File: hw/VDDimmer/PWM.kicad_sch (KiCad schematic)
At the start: 23 parts, among them J3 CH1 V+/LED-, J4 CH2 V+/LED-, J5 CH3 V+/LED-, J6 CH4 V+/LED-, Q1 20N06, Q2 20N06, Q3 20N06, Q4 20N06, U4 74HCT125

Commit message: Schematic pass: MPN/LCSC/Manufacturer on all 79 sourced parts
F1 -> "8A 250V", U3 -> "BL1117-33CX", J2 -> "VIN 12V" (was "VIN 9-24V",
which invited 24 V into an 18 V TVS). R11/R12 values cleaned to "47R" with
the DNP intent moved into the Assembly field. ERC still 0 violations.

Every sourced part now carries MPN, LCSC and Manufacturer, plus an Assembly
note anywhere the choice needs explaining - why D5 is an SMBJ18A, why R30's
current rating still needs checking, why L1 is candidate-only.

Two things this pass could NOT do, both because no MCP tool writes them:

- KiCad's (dnp yes) attribute. R11 and R12 must be flagged in the GUI; their
  Assembly fields say so. All five text-only DNPs were in this state, but
  L3/C20/R31 are now fitted by decision, so only R11/R12 remain.
- Fields on units 2-5 of a multi-unit symbol. Konnect writes unit 1 only,
  where the GUI propagates to all units. U4/U5 are 5-unit 74HCT125s, so
  grouping a BOM by MPN splits U5 into two lines and would order 3 of a
  2-off part. tools/export-bom.sh groups by Value+Footprint instead, which
  collapses correctly - 49 lines, 96 parts, and the 15 lines without an LCSC
  are exactly the mounting holes and hand-fit connectors.

Also checked and left alone: the U4/U5 symbol's lib_id is 74AHCT125 while its
value is 74HCT125. AHCT would be the conventional WS2812 level shifter, but
JLC has 70 of it in SO-14 against 88,003 of the HCT part, and HCT is fine here
- TTL inputs, 15 ns against 300 ns bit times. The value is the buyable intent.

Co-Authored-By: Claude Opus 5 (1M context) <noreply@anthropic.com>
Claude-Session: https://claude.ai/code/session_01QsYnM2qRBWQsyKPH1v7rLR
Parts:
- C50: LCSC (none) -> C15850; MPN (none) -> CL21A106KAYNNNE; Manufacturer (none) -> Samsung Electro-Mechanics
- C51: LCSC (none) -> C14663; MPN (none) -> CC0603KRX7R9BB104; Manufacturer (none) -> YAGEO
- D1, D2, D3, D4: LCSC (none) -> C8678; MPN (none) -> SS34; Manufacturer (none) -> MDD
- Q1: Assembly (none) -> Rds(on) 29 mOhm at the 4.5 V the 74HCT125 drives, not the 1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; LCSC (none) -> C2890395; MPN (none) -> 20N06; Manufacturer (none) -> UMW
- Q2, Q3, Q4: LCSC (none) -> C2890395; MPN (none) -> 20N06; Manufacturer (none) -> UMW
- R1, R2, R3, R4: LCSC (none) -> C17557; MPN (none) -> 0805W8F2200T5E; Manufacturer (none) -> UNI-ROYAL
- R5, R6, R7, R8: LCSC (none) -> C17414; MPN (none) -> 0805W8F1002T5E; Manufacturer (none) -> UNI-ROYAL
- U4: LCSC (none) -> C5962; MPN (none) -> 74HCT125D,653; Manufacturer (none) -> Nexperia

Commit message: Fix six drill defects, fit the I2C pull-ups, add the board ID
Drill defects
-------------
hole_to_hole and holes_co_located are downgraded to warning in .kicad_pro, so
the board reported "DRC 0 errors" while carrying five hole_to_hole and one
holes_co_located -- two of them with physically overlapping drills. Same shape
of trap as the split-net lesson already in HANDOFF.

Five vias deleted, each proven non-load-bearing first by checking which track
endpoints actually land on it. In every overlapping pair only one via carried a
track; the other was a bare stitching via with its twin 0.1-0.5 mm away.
d85c5d26 was redundant by construction -- 1 mm from J2's PTH GND pad, which
already ties both layers. afb88017 was an exact duplicate of a14092cd.
Afterwards GND is still one connected group, the split-net count is unchanged
at 12, and via count went 192 -> 187.

I2C pull-ups (R45, R46)
-----------------------
4.7k 0805, C17673, per the 2026-08-29 decision. Verified against the exported
netlist rather than the tools' return values, because the pins are tied with a
plain +3V3 net label -- the convention J13's own supply pin uses on this sheet.
Had that not merged with the power net the pull-ups would have pulled to
nothing, which is the silent failure the decision existed to prevent.

  +3V3          15 nodes  ... J13.1 R43.1 R44.1 R45.1 R46.1 U1.2 U3.2
  /MCU/I2C_SDA   3 nodes  J13.3  R45.2  U1.20
  /MCU/I2C_SCL   3 nodes  J13.4  R46.2  U1.18

The taps run on B.Cu because ADDR1_DIN crosses the whole board on F.Cu at
y=96.33, x 149.35-168.60, walling +3V3 (which reaches J13.1 at y=95) off from
the I2C lines at y=100.14 and 102.67. There is no F.Cu-only path; going round
its east end costs ~30 mm and still needs via hops over the GATE_IN verticals.
B.Cu there is bare GND pour and J13's pads 1/3/4 are through-hole, so they are
reachable from below with no via at that end.

Both parts are rotated 180 deg. They arrive with pad 1 (+3V3) west, which would
force the SDA return to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
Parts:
- U4: LCSC (none) -> C5962; MPN (none) -> 74HCT125D,653; Manufacturer (none) -> Nexperia
- U4: LCSC C5962 -> (none); MPN 74HCT125D,653 -> (none); Manufacturer Nexperia -> (none)

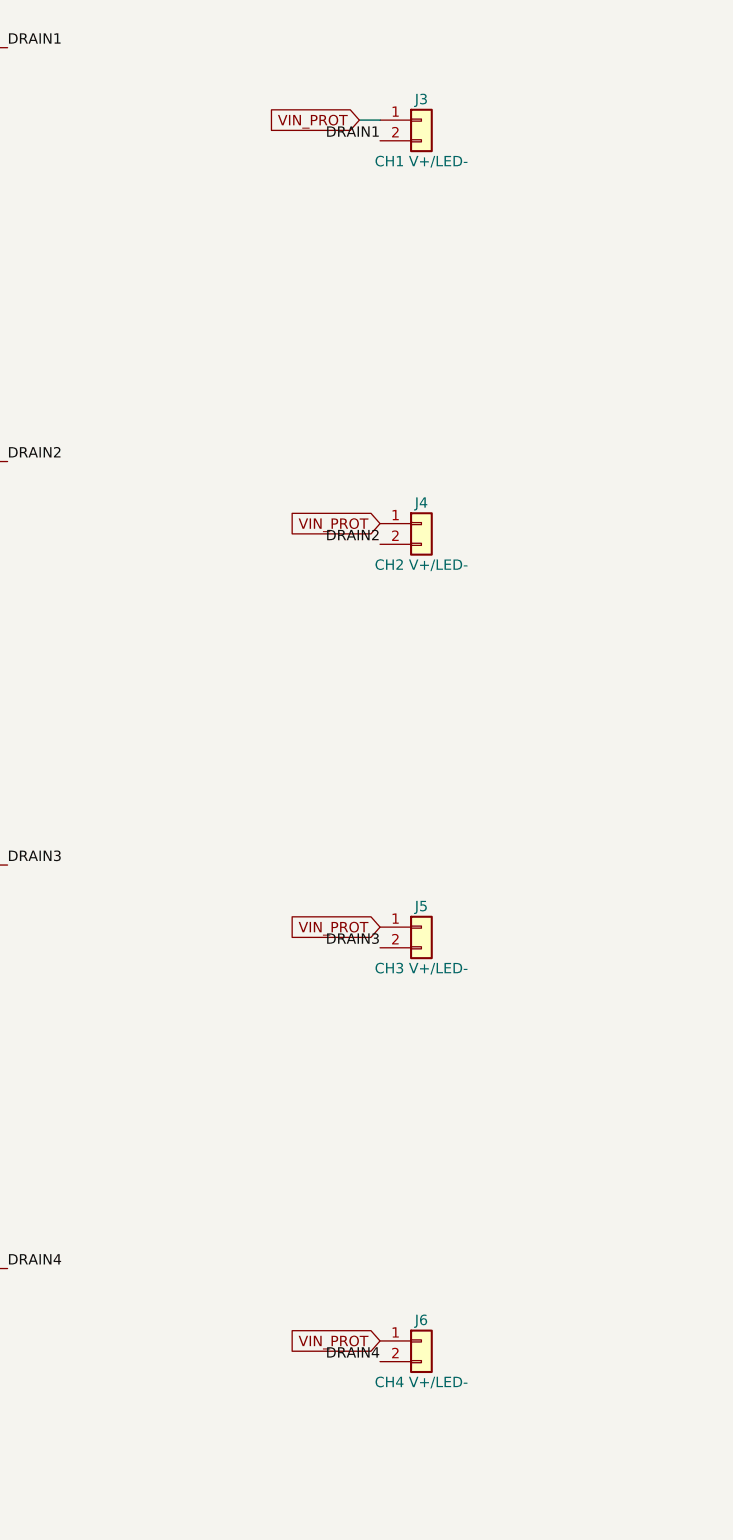
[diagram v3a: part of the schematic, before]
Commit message: Swap J3-J6 pin order: pin 1 is now the LED- return
Rev A has pin 1 = VIN_PROT, so grounding pin 1 on a Rev A board is a dead
short across the supply. Rev B reverses it: pin 1 = DRAINn (LED-), pin 2 =
VIN_PROT (V+), per spec section 6.

Implemented as a label exchange -- the sheet places a VIN_PROT global label
and a DRAINn local label directly on the pin coordinates -- plus removal of
J3's now-redundant 2.54 mm stub wire, so all four connectors are wired
identically.

Also swapped the Value strings ("CH1 V+/LED-" -> "CH1 LED-/V+"), which the
plan does not mention but which encode the pin order on the schematic face.
Leaving them would have left the drawing asserting the Rev A polarity -- the
same wrong-polarity hazard this task exists to remove.

Verified by netlist diff, not by eye: 81 nets before and after, none added or
removed, and the only membership changes are the eight intended pin moves.

Co-Authored-By: Claude Opus 5 (1M context) <noreply@anthropic.com>
Claude-Session: https://claude.ai/code/session_01YZHVU8aymL4RkLeCfwomwj
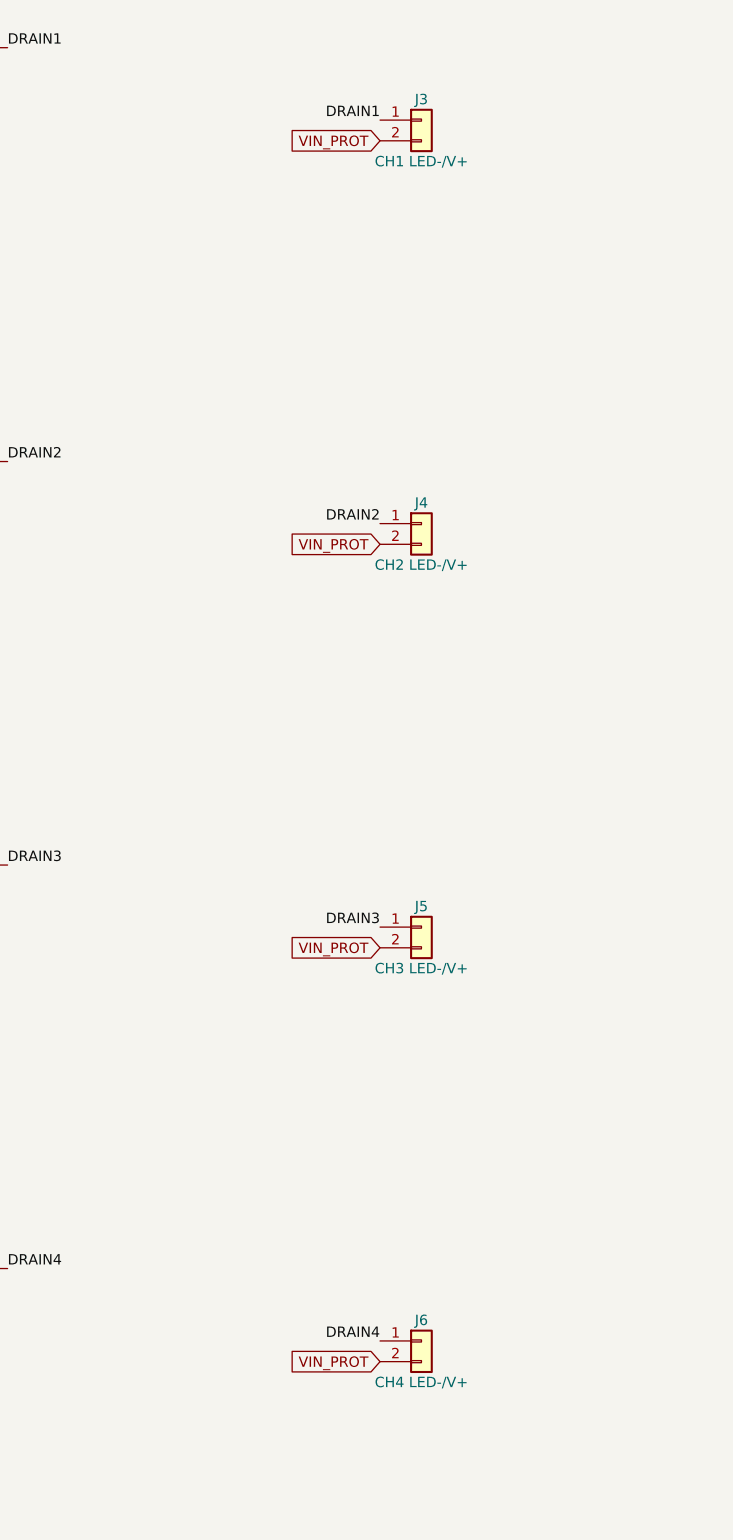
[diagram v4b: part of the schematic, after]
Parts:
- J3: value CH1 V+/LED- -> CH1 LED-/V+
- J4: value CH2 V+/LED- -> CH2 LED-/V+
- J5: value CH3 V+/LED- -> CH3 LED-/V+
- J6: value CH4 V+/LED- -> CH4 LED-/V+
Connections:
- net DRAIN1: now also J3.1 (Pin_1); no longer J3.2 (Pin_2)
- net DRAIN2: now also J4.1 (Pin_1); no longer J4.2 (Pin_2)
- net DRAIN3: now also J5.1 (Pin_1); no longer J5.2 (Pin_2)
- net DRAIN4: now also J6.1 (Pin_1); no longer J6.2 (Pin_2)
- net VIN_PROT: now also J3.2 (Pin_2), J4.2 (Pin_2), J5.2 (Pin_2), J6.2 (Pin_2); no longer J3.1 (Pin_1), J4.1 (Pin_1), J5.1 (Pin_1), J6.1 (Pin_1)

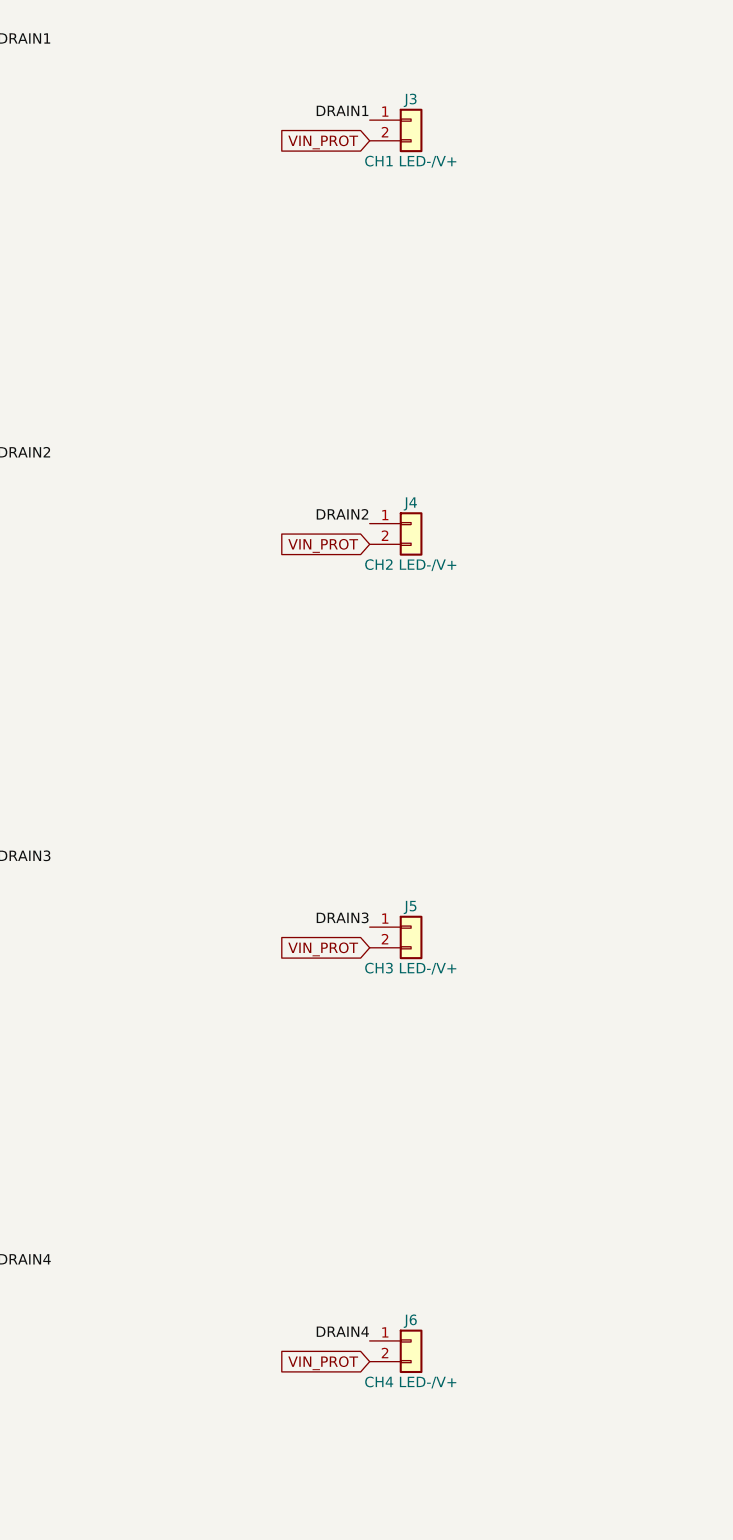
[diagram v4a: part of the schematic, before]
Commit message: Revert J3-J6 to Rev A's pin order and enlarge the polarity marks
The Molex 22-05-3021 keyway puts a pre-plugged lamp's + on pin 1, so Rev B
keeps Rev A's order: pin 1 = VIN_PROT, pin 2 = DRAINn. This reverses Task 4
(55af04c). One harness now fits both revisions.

Schematic: the eight J3-J6 labels are exchanged back and the Values restored to
"CHn V+/LED-". Checked by netlist diff: 81 nets and 294 pins before and after,
and the only changes are the eight intended pin moves. ERC: 0 errors.

PCB: eight new polarity marks at 1.5 mm (were 0.8 mm), + beside pin 1 and -
beside pin 2, plus a 3 mm "REV B". Konnect cannot delete or edit board text,
so tools/revb_silk_pass.py finishes the job from KiCad's scripting console. It
removes the old marks and "Rev A" by UUID, sets a 0.3 mm stroke, and moves the
title off the buck cluster. Tested on a scratch copy: silk_overlap 28 -> 14,
silk_over_copper 9 -> 5, no new silk violations. The pad nets still need F8.

Spec 5.1, Rev B design 6 + decision 9 and HANDOFF 1 are amended explicitly.

Co-Authored-By: Claude Opus 5 (1M context) <noreply@anthropic.com>
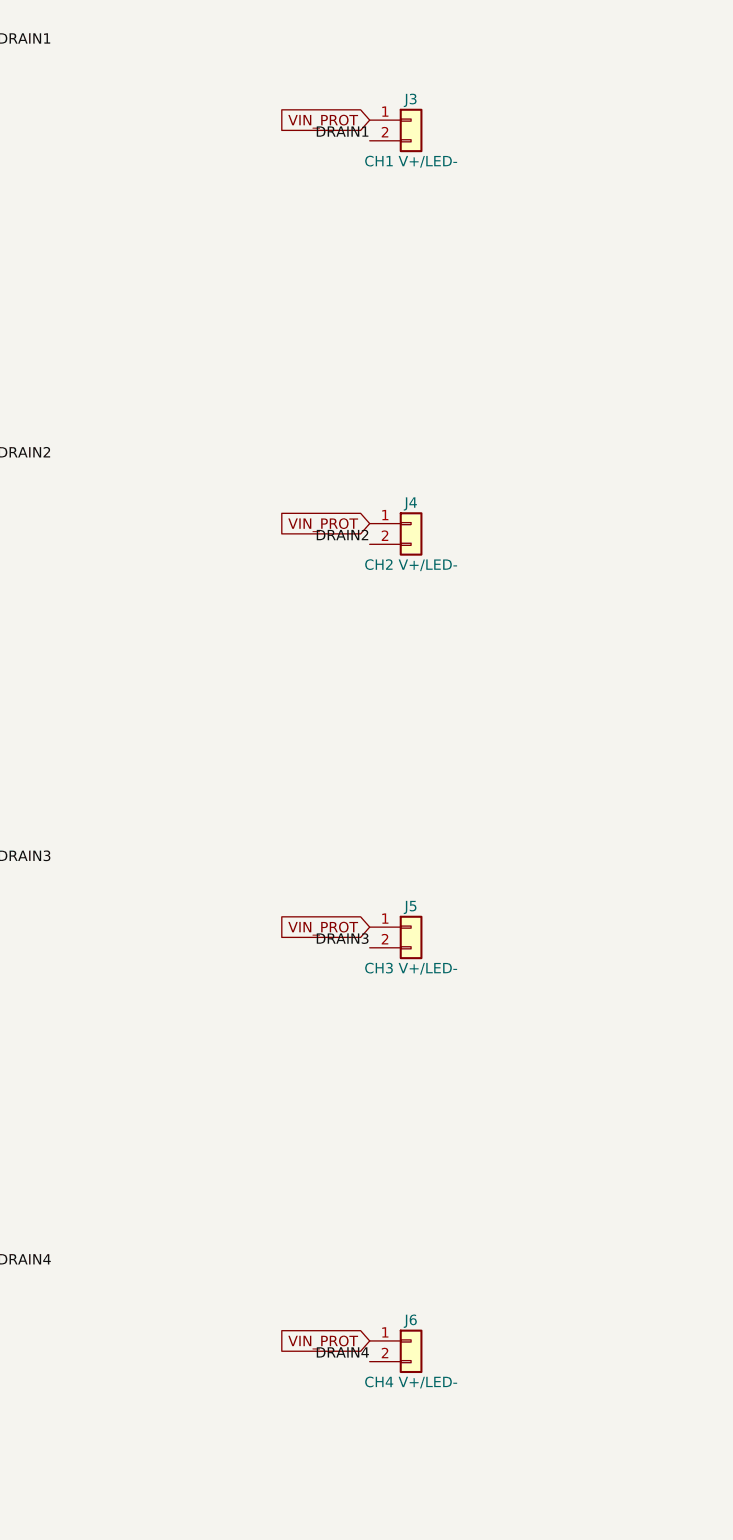
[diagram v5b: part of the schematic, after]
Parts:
- J3: value CH1 LED-/V+ -> CH1 V+/LED-
- J4: value CH2 LED-/V+ -> CH2 V+/LED-
- J5: value CH3 LED-/V+ -> CH3 V+/LED-
- J6: value CH4 LED-/V+ -> CH4 V+/LED-
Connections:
- net DRAIN1: now also J3.2 (Pin_2); no longer J3.1 (Pin_1)
- net DRAIN2: now also J4.2 (Pin_2); no longer J4.1 (Pin_1)
- net DRAIN3: now also J5.2 (Pin_2); no longer J5.1 (Pin_1)
- net DRAIN4: now also J6.2 (Pin_2); no longer J6.1 (Pin_1)
- net VIN_PROT: now also J3.1 (Pin_1), J4.1 (Pin_1), J5.1 (Pin_1), J6.1 (Pin_1); no longer J3.2 (Pin_2), J4.2 (Pin_2), J5.2 (Pin_2), J6.2 (Pin_2)
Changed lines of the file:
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@@
 	)
 	(label "DRAIN1"
-		(at 245.11 58.42 180)
+		(at 245.11 60.96 180)
 		(effects
 			(font
@@
 	)
 	(label "DRAIN2"
-		(at 245.11 107.95 180)
+		(at 245.11 110.49 180)
 		(effects
 			(font
@@
 	)
 	(label "DRAIN3"
-		(at 245.11 157.48 180)
+		(at 245.11 160.02 180)
 		(effects
 			(font
@@
 	)
 	(label "DRAIN4"
-		(at 245.11 208.28 180)
+		(at 245.11 210.82 180)
 		(effects
 			(font
@@
 	(global_label "VIN_PROT"
 		(shape input)
-		(at 245.11 60.96 180)
+		(at 245.11 58.42 180)
 		(effects
 			(font
@@
 	(global_label "VIN_PROT"
 		(shape input)
-		(at 245.11 110.49 180)
+		(at 245.11 107.95 180)
 		(effects
 			(font
@@
 	(global_label "VIN_PROT"
 		(shape input)
-		(at 245.11 160.02 180)
+		(at 245.11 157.48 180)
 		(effects
 			(font
@@
 	(global_label "VIN_PROT"
 		(shape input)
-		(at 245.11 210.82 180)
+		(at 245.11 208.28 180)
 		(effects
 			(font
@@
 			)
 		)
-		(property "Value" "CH2 LED-/V+"
+		(property "Value" "CH2 V+/LED-"
 			(at 250.19 113.03 0)
 			(show_name no)
@@
 			)
 		)
-		(property "Value" "CH4 LED-/V+"
+		(property "Value" "CH4 V+/LED-"
 			(at 250.19 213.36 0)
 			(show_name no)
@@
 			)
 		)
-		(property "Value" "CH3 LED-/V+"
+		(property "Value" "CH3 V+/LED-"
 			(at 250.19 162.56 0)
 			(show_name no)
@@
 			)
 		)
-		(property "Value" "CH1 LED-/V+"
+		(property "Value" "CH1 V+/LED-"
 			(at 250.19 63.5 0)
 			(show_name no)
